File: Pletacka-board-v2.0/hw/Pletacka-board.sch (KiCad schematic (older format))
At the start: 40 parts, among them SW1 Reset_Button, SW2 User_Button, U1 TPS54231D, U2 EL357N(A)(TA)-G, U3 EL357N(A)(TA)-G

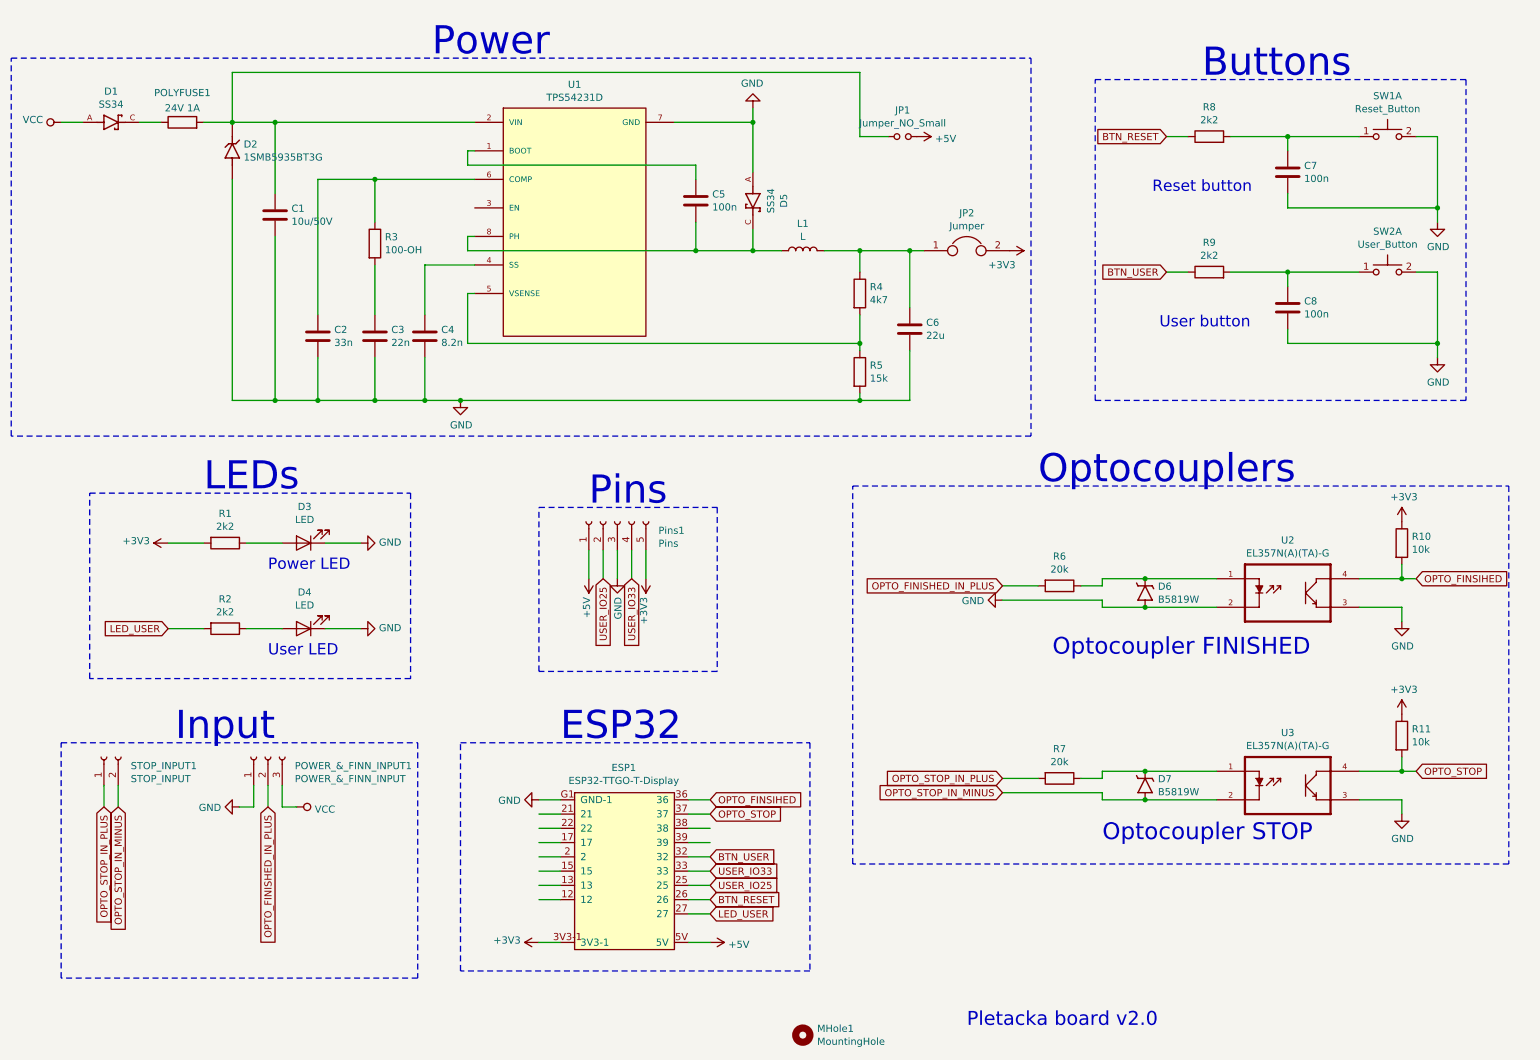
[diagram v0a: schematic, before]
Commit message: Remove buttons - chage board
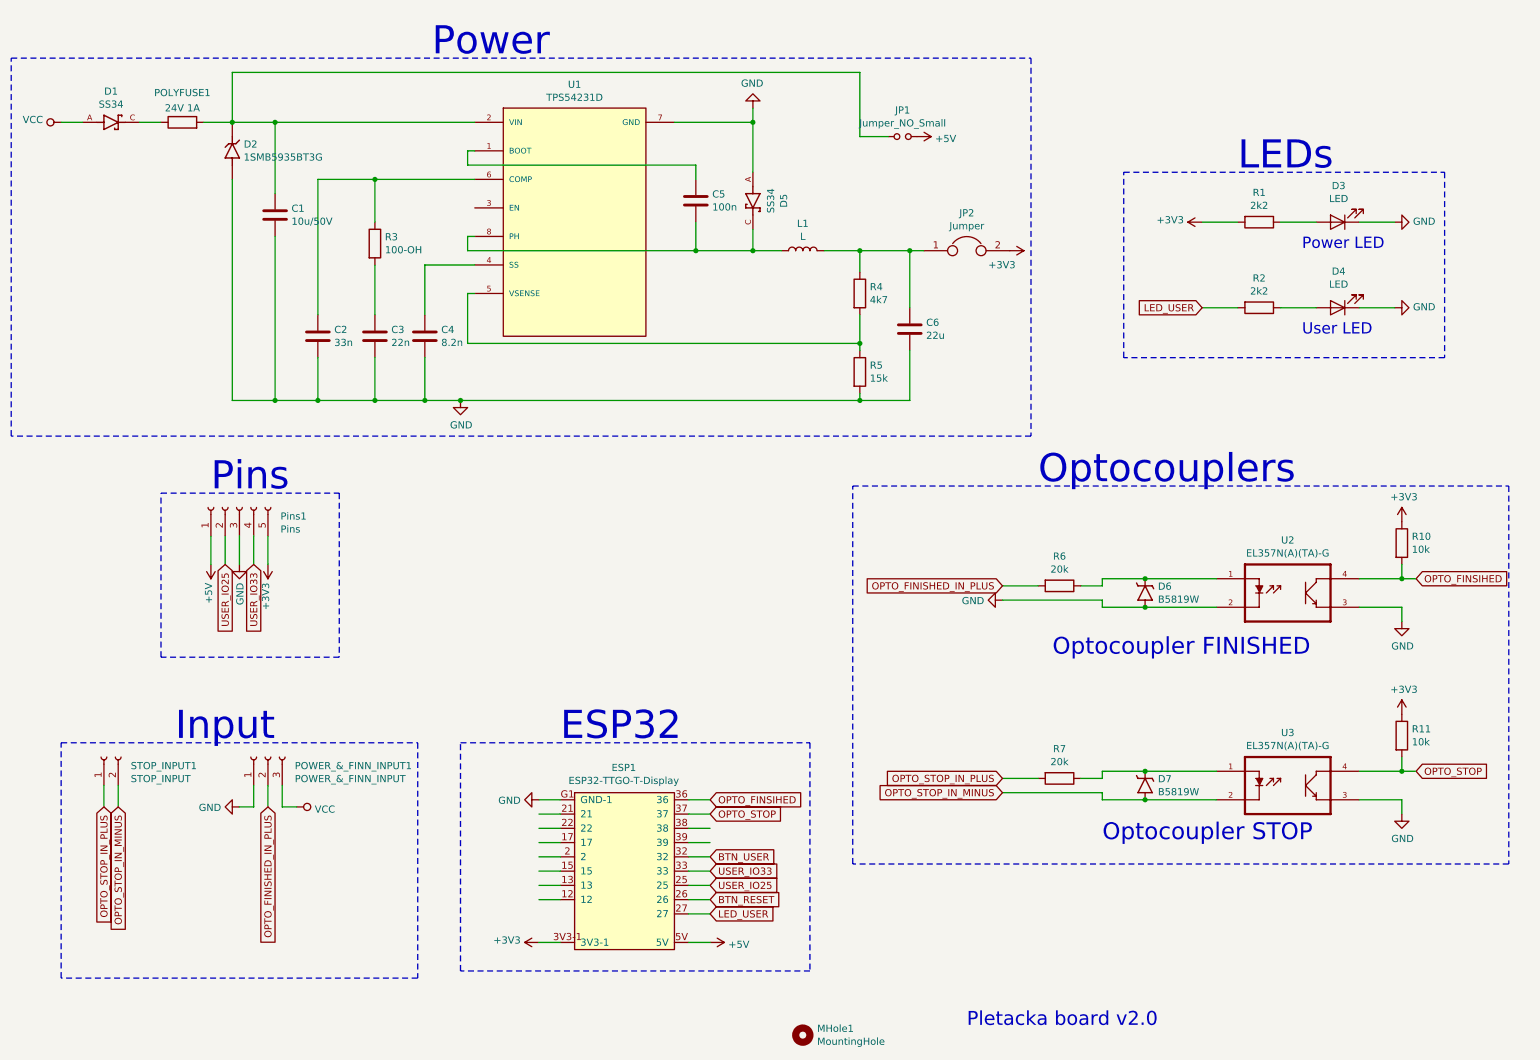
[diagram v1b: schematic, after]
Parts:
- removed C7, C8: 100n, Capacitor_SMD:C_0603_1608Metric, symbol Device:C
- removed R8, R9: 2k2, Resistor_SMD:R_0603_1608Metric, symbol Device:R
- removed SW1: Reset_Button, Button_SMD:Button_SMD_10mm, symbol Switch:SW_Push_Dual_x2
- removed SW2: User_Button, Button_SMD:Button_SMD_10mm, symbol Switch:SW_Push_Dual_x2
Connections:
- wire segments 138 -> 120
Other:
- note removed: "Buttons"
- note removed: "Reset button"
- note removed: "User button"
- moved on the sheet: D3, D4, Pins1, R1, R2
